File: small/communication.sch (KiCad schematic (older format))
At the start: 10 parts, among them J5 Conn_02x04_Odd_Even, U9 ISO1540

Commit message: simcard colder changed to 78800-0001
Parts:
- C27, C28: LCSC (none) -> C14663
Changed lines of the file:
@@
 F 5 "0,019 €" H 3100 3300 50  0001 C CNN "Price"
 F 6 "Mouser" H 3100 3300 50  0001 C CNN "Website"
+F 7 "C14663" H 3100 3300 50  0001 C CNN "LCSC"
 	1    3100 3300
 	1    0    0    -1
@@
 F 5 "0,019 €" H 5675 2875 50  0001 C CNN "Price"
 F 6 "Mouser" H 5675 2875 50  0001 C CNN "Website"
+F 7 "C14663" H 5675 2875 50  0001 C CNN "LCSC"
 	1    5675 2875
 	1    0    0    -1

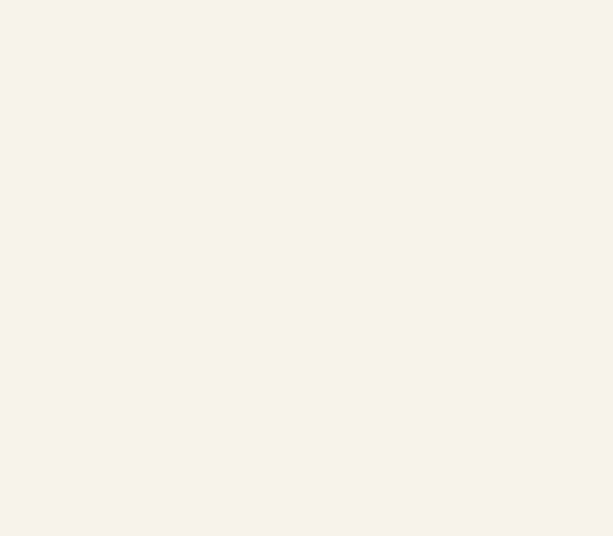
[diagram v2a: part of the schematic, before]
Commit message: connector rotated.
added rs485 output.

TODO: add bluetooth port.
check all parts
preaper bom list
prepare mouser list
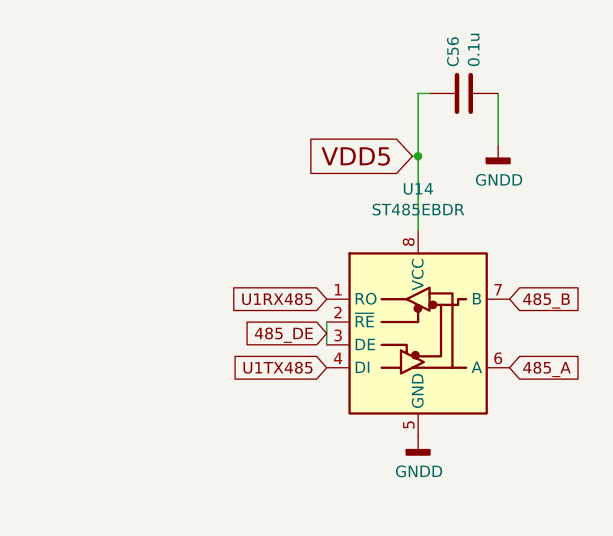
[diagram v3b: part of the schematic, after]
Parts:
- added C56: 0.1u, Capacitor_SMD:C_0603_1608Metric, symbol Device:C
- added U14: ST485EBDR, Package_SO:SOIC-8_3.9x4.9mm_P1.27mm, symbol Interface_UART:ST485EBDR
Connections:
- net GNDD: now also C56.2, U14.5 (GND)
- net VDD5: now also C56.1, U14.8 (VCC)
- new net 485_A: U14.6 (A)
- new net 485_B: U14.7 (B)
- new net 485_DE: U14.2 (~RE), U14.3 (DE)
- new net U1RX485: U14.1 (RO)
- new net U1TX485: U14.4 (DI)
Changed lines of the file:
@@
 	1    0    0    -1
 $EndComp
+$Comp
+L Interface_UART:ST485EBDR U14
+U 1 1 606D84B9
+P 8350 2825
+F 0 "U14" H 8350 3406 50  0000 C CNN
+F 1 "ST485EBDR" H 8350 3315 50  0000 C CNN
+F 2 "Package_SO:SOIC-8_3.9x4.9mm_P1.27mm" H 8350 1925 50  0001 C CNN
+F 3 "http://www.st.com/resource/en/datasheet/st485eb.pdf" H 8350 2875 50  0001 C CNN
+	1    8350 2825
+	1    0    0    -1
+$EndComp
+Text GLabel 7950 3025 0    50   Input ~ 0
+U1TX485
+Text GLabel 7950 2725 0    50   Input ~ 0
+U1RX485
+Wire Wire Line
+	7950 2925 7950 2825
+Text GLabel 7950 2875 0    50   Input ~ 0
+485_DE
+Text GLabel 8750 3025 2    50   Input ~ 0
+485_A
+Text GLabel 8750 2725 2    50   Input ~ 0
+485_B
+$Comp
+L power:GNDD #PWR0124
+U 1 1 606E725A
+P 8350 3325
+F 0 "#PWR0124" H 8350 3075 50  0001 C CNN
+F 1 "GNDD" H 8354 3170 50  0000 C CNN
+F 2 "" H 8350 3325 50  0001 C CNN
+F 3 "" H 8350 3325 50  0001 C CNN
+	1    8350 3325
+	1    0    0    -1
+$EndComp
+Text GLabel 8325 2100 0    79   Input ~ 0
+VDD5
+$Comp
+L power:GNDD #PWR0185
+U 1 1 606EB876
+P 8700 2050
+F 0 "#PWR0185" H 8700 1800 50  0001 C CNN
+F 1 "GNDD" H 8704 1895 50  0000 C CNN
+F 2 "" H 8700 2050 50  0001 C CNN
+F 3 "" H 8700 2050 50  0001 C CNN
+	1    8700 2050
+	1    0    0    -1
+$EndComp
+Wire Wire Line
+	8700 1825 8700 2050
+$Comp
+L Device:C C?
+U 1 1 606EAE77
+P 8550 1825
+AR Path="/606EAE77" Ref="C?"  Part="1"
+AR Path="/608144C5/606EAE77" Ref="C56"  Part="1"
+F 0 "C56" H 8665 1871 50  0000 L CNN
+F 1 "0.1u" H 8665 1780 50  0000 L CNN
+F 2 "Capacitor_SMD:C_0603_1608Metric" H 8588 1675 50  0001 C CNN
+F 3 "https://eu.mouser.com/datasheet/2/445/885012207098-1727748.pdf" H 8550 1825 50  0001 C CNN
+F 4 "885012207098" H 8550 1825 50  0001 C CNN "Mpn"
+F 5 "0,019 €" H 8550 1825 50  0001 C CNN "Price"
+F 6 "Mouser" H 8550 1825 50  0001 C CNN "Website"
+F 7 "C14663" H 8550 1825 50  0001 C CNN "LCSC"
+	1    8550 1825
+	0    -1   -1   0
+$EndComp
+Wire Wire Line
+	8350 2100 8325 2100
+Wire Wire Line
+	8350 2425 8350 2100
+Wire Wire Line
+	8350 2100 8350 1825
+Wire Wire Line
+	8350 1825 8400 1825
+Connection ~ 8350 2100
 $EndSCHEMATC

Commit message: GPS connector moved,
antenna matching networks removed

SUPERCAPACITOR from jlpcb used.
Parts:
- added D14: PSM712-LF-T7, Package_TO_SOT_SMD:SOT-23, symbol Diode:SM712_SOT23
- added JP3: Jumper, Jumper:SolderJumper-2_P1.3mm_Open_RoundedPad1.0x1.5mm, symbol Device:Jumper
- R12: value R -> 120
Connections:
- net 485_A: now also R12.2, D14.1 (A1)
- net 485_B: now also R12.1, D14.2 (A2)
- net GND_ISO: no longer C28.2, J5.7 (Pin_7)
- net SCL_ISO: no longer J5.5 (Pin_5)
- net SDA_ISO: no longer J5.3 (Pin_3)
- net VDD5: now also C28.1, J5.1 (Pin_1), JP3.1; no longer R12.1
- net VDD_ISO: now also JP3.2; no longer C28.1, J5.1 (Pin_1), R12.2
- net GNDD renamed GND
- net GND: now also C28.2, J5.3 (Pin_3), D14.3 (common)
- net SCL1 renamed SCL2
- net SDA1 renamed SDA2
- new net U2RX: J5.5 (Pin_5)
- new net U2TX: J5.7 (Pin_7)
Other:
- moved on the sheet: C28
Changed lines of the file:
@@
 Wire Wire Line
 	4125 2725 4375 2725
-Wire Wire Line
-	4375 2725 4375 2625
-$Comp
-L Device:R R?
-U 1 1 60818F85
-P 4375 2475
-AR Path="/60818F85" Ref="R?"  Part="1"
-AR Path="/608144C5/60818F85" Ref="R12"  Part="1"
-F 0 "R12" H 4445 2521 50  0000 L CNN
-F 1 "R" H 4445 2430 50  0000 L CNN
-F 2 "Resistor_SMD:R_0805_2012Metric" V 4305 2475 50  0001 C CNN
-F 3 "" H 4375 2475 50  0001 C CNN
-	1    4375 2475
-	1    0    0    -1
-$EndComp
 Connection ~ 4375 3025
 Connection ~ 4375 2725
@@
 Text Label 4450 2925 0    50   ~ 0
 SCL_ISO
-$Comp
-L Connector_Generic:Conn_02x04_Odd_Even J?
-U 1 1 60818F91
-P 5150 2825
-AR Path="/60818F91" Ref="J?"  Part="1"
-AR Path="/608144C5/60818F91" Ref="J5"  Part="1"
-F 0 "J5" H 5200 3142 50  0000 C CNN
-F 1 "Conn_02x04_Odd_Even" H 5200 3051 50  0000 C CNN
-F 2 "Connector_PinHeader_2.54mm:PinHeader_2x04_P2.54mm_Vertical" H 5150 2825 50  0001 C CNN
-F 3 "~" H 5150 2825 50  0001 C CNN
-F 4 "Connector unknown" H 5150 2825 50  0001 C CNN "Mpn"
-	1    5150 2825
-	1    0    0    -1
-$EndComp
-Wire Wire Line
-	5450 2725 4950 2725
 Wire Wire Line
 	4375 2725 4950 2725
-Connection ~ 4950 2725
 Wire Wire Line
 	4125 2825 4775 2825
 Wire Wire Line
-	4950 2825 5450 2825
-Connection ~ 4950 2825
-Wire Wire Line
 	4125 2925 4850 2925
 Wire Wire Line
-	4950 2925 5450 2925
-Connection ~ 4950 2925
-Wire Wire Line
-	5450 3025 4950 3025
-Wire Wire Line
 	4375 3025 4950 3025
-Connection ~ 4950 3025
 Text Notes 5050 2450 0    50   ~ 0
 i2c-iso
@@
 L Device:C C?
 U 1 1 60818FB1
-P 5675 2875
+P 6175 2875
 AR Path="/60818FB1" Ref="C?"  Part="1"
 AR Path="/608144C5/60818FB1" Ref="C28"  Part="1"
-F 0 "C28" H 5790 2921 50  0000 L CNN
-F 1 "0.1u" H 5790 2830 50  0000 L CNN
-F 2 "Capacitor_SMD:C_0603_1608Metric" H 5713 2725 50  0001 C CNN
-F 3 "https://eu.mouser.com/datasheet/2/445/885012207098-1727748.pdf" H 5675 2875 50  0001 C CNN
-F 4 "885012207098" H 5675 2875 50  0001 C CNN "Mpn"
-F 5 "0,019 €" H 5675 2875 50  0001 C CNN "Price"
-F 6 "Mouser" H 5675 2875 50  0001 C CNN "Website"
-F 7 "C14663" H 5675 2875 50  0001 C CNN "LCSC"
-	1    5675 2875
-	1    0    0    -1
-$EndComp
-Wire Wire Line
-	5450 2725 5675 2725
-Connection ~ 5450 2725
-Wire Wire Line
-	5675 3025 5450 3025
-Connection ~ 5450 3025
+F 0 "C28" H 6290 2921 50  0000 L CNN
+F 1 "0.1u" H 6290 2830 50  0000 L CNN
+F 2 "Capacitor_SMD:C_0603_1608Metric" H 6213 2725 50  0001 C CNN
+F 3 "https://eu.mouser.com/datasheet/2/445/885012207098-1727748.pdf" H 6175 2875 50  0001 C CNN
+F 4 "885012207098" H 6175 2875 50  0001 C CNN "Mpn"
+F 5 "0,019 €" H 6175 2875 50  0001 C CNN "Price"
+F 6 "Mouser" H 6175 2875 50  0001 C CNN "Website"
+F 7 "C14663" H 6175 2875 50  0001 C CNN "LCSC"
+	1    6175 2875
+	1    0    0    -1
+$EndComp
 Wire Wire Line
 	4775 2825 4775 2375
@@
 	4775 2825 4950 2825
 Wire Wire Line
-	4850 2925 4850 2450
+	4850 2925 4850 2575
 Connection ~ 4850 2925
 Wire Wire Line
@@
 	1    0    0    -1
 $EndComp
-Wire Wire Line
-	4850 2450 4900 2450
-Wire Wire Line
-	4900 2450 4900 2375
 Connection ~ 3100 3450
 Wire Wire Line
@@
 	3100 2725 3100 3150
 Text GLabel 2825 2825 0    50   Input ~ 0
-SDA1
+SDA2
 Text GLabel 2825 2925 0    50   Input ~ 0
-SCL1
-Wire Wire Line
-	4375 2325 4375 2075
+SCL2
 Wire Wire Line
 	4375 2075 4775 2075
@@
 Text GLabel 7950 2875 0    50   Input ~ 0
 485_DE
-Text GLabel 8750 3025 2    50   Input ~ 0
+Text GLabel 9525 3025 2    50   Input ~ 0
 485_A
-Text GLabel 8750 2725 2    50   Input ~ 0
+Text GLabel 9525 2725 2    50   Input ~ 0
 485_B
 $Comp
@@
 	8350 1825 8400 1825
 Connection ~ 8350 2100
+$Comp
+L Device:Jumper JP3
+U 1 1 602848D0
+P 4375 2425
+F 0 "JP3" V 4329 2552 50  0000 L CNN
+F 1 "Jumper" V 4420 2552 50  0000 L CNN
+F 2 "Jumper:SolderJumper-2_P1.3mm_Open_RoundedPad1.0x1.5mm" H 4375 2425 50  0001 C CNN
+F 3 "~" H 4375 2425 50  0001 C CNN
+	1    4375 2425
+	0    1    1    0
+$EndComp
+Wire Wire Line
+	4375 2125 4375 2075
+Wire Wire Line
+	4900 2075 5450 2075
+Wire Wire Line
+	5450 2075 5450 2725
+Connection ~ 4900 2075
+Wire Wire Line
+	5950 2825 5950 3025
+Wire Wire Line
+	5950 3025 6175 3025
+$Comp
+L power:GNDD #PWR0187
+U 1 1 6028DDBE
+P 6175 3025
+F 0 "#PWR0187" H 6175 2775 50  0001 C CNN
+F 1 "GNDD" H 6179 2870 50  0000 C CNN
+F 2 "" H 6175 3025 50  0001 C CNN
+F 3 "" H 6175 3025 50  0001 C CNN
+	1    6175 3025
+	1    0    0    -1
+$EndComp
+Connection ~ 6175 3025
+Wire Wire Line
+	5450 2825 5950 2825
+Wire Wire Line
+	5450 2725 6175 2725
+Text GLabel 5450 3025 2    50   Input ~ 0
+U2TX
+Text GLabel 5450 2925 2    50   Input ~ 0
+U2RX
+$Comp
+L Connector_Generic:Conn_02x04_Odd_Even J?
+U 1 1 60818F91
+P 5250 2825
+AR Path="/60818F91" Ref="J?"  Part="1"
+AR Path="/608144C5/60818F91" Ref="J5"  Part="1"
+F 0 "J5" H 5300 3142 50  0000 C CNN
+F 1 "Conn_02x04_Odd_Even" H 5300 3051 50  0000 C CNN
+F 2 "Connector_PinHeader_2.54mm:PinHeader_2x04_P2.54mm_Vertical" H 5250 2825 50  0001 C CNN
+F 3 "~" H 5250 2825 50  0001 C CNN
+F 4 "Connector unknown" H 5250 2825 50  0001 C CNN "Mpn"
+	1    5250 2825
+	-1   0    0    -1
+$EndComp
+Connection ~ 5450 2725
+$Comp
+L power:GND #PWR0188
+U 1 1 60296547
+P 3600 1800
+F 0 "#PWR0188" H 3600 1550 50  0001 C CNN
+F 1 "GND" H 3605 1627 50  0000 C CNN
+F 2 "" H 3600 1800 50  0001 C CNN
+F 3 "" H 3600 1800 50  0001 C CNN
+	1    3600 1800
+	1    0    0    -1
+$EndComp
+$Comp
+L power:GNDD #PWR0189
+U 1 1 60296AF3
+P 3825 1800
+F 0 "#PWR0189" H 3825 1550 50  0001 C CNN
+F 1 "GNDD" H 3829 1645 50  0000 C CNN
+F 2 "" H 3825 1800 50  0001 C CNN
+F 3 "" H 3825 1800 50  0001 C CNN
+	1    3825 1800
+	1    0    0    -1
+$EndComp
+Wire Wire Line
+	3825 1800 3600 1800
+$Comp
+L Device:R R12
+U 1 1 6035DB1F
+P 9250 2875
+F 0 "R12" H 9320 2921 50  0000 L CNN
+F 1 "120" H 9320 2830 50  0000 L CNN
+F 2 "Resistor_SMD:R_0805_2012Metric" V 9180 2875 50  0001 C CNN
+F 3 "https://datasheet.lcsc.com/szlcsc/Uniroyal-Elec-0805W8F1200T5E_C17437.pdf" H 9250 2875 50  0001 C CNN
+	1    9250 2875
+	1    0    0    -1
+$EndComp
+Wire Wire Line
+	8750 2725 9250 2725
+Connection ~ 9250 2725
+Wire Wire Line
+	9250 2725 9475 2725
+Wire Wire Line
+	9525 3025 9250 3025
+Connection ~ 9250 3025
+Wire Wire Line
+	9250 3025 8775 3025
+$Comp
+L Diode:SM712_SOT23 D14
+U 1 1 603613E9
+P 9125 3425
+F 0 "D14" H 9125 3641 50  0000 C CNN
+F 1 "PSM712-LF-T7" H 9125 3550 50  0000 C CNN
+F 2 "Package_TO_SOT_SMD:SOT-23" H 9125 3075 50  0001 C CNN
+F 3 "https://datasheet.lcsc.com/szlcsc/ProTek-Devices-PSM712-LF-T7_C32677.pdf" H 8975 3425 50  0001 C CNN
+F 4 "C32677" H 9125 3425 50  0001 C CNN "LCSC"
+F 5 "0.3704" H 9125 3425 50  0001 C CNN "Price"
+F 6 "PSM712-LF-T7" H 9125 3425 50  0001 C CNN "MPN"
+	1    9125 3425
+	1    0    0    -1
+$EndComp
+$Comp
+L power:GNDD #PWR0184
+U 1 1 60362763
+P 9125 3650
+F 0 "#PWR0184" H 9125 3400 50  0001 C CNN
+F 1 "GNDD" H 9129 3495 50  0000 C CNN
+F 2 "" H 9125 3650 50  0001 C CNN
+F 3 "" H 9125 3650 50  0001 C CNN
+	1    9125 3650
+	1    0    0    -1
+$EndComp
+Wire Wire Line
+	9125 3575 9125 3650
+Wire Wire Line
+	8775 3425 8775 3025
+Connection ~ 8775 3025
+Wire Wire Line
+	8775 3025 8750 3025
+Wire Wire Line
+	9475 3425 9475 2725
+Connection ~ 9475 2725
+Wire Wire Line
+	9475 2725 9525 2725
+Wire Wire Line
+	4900 2575 4850 2575
+Wire Wire Line
+	4900 2375 4900 2575
 $EndSCHEMATC

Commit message: BOM updated
Layout changed
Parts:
- C27, C28, C56: MPN (none) -> CC0603KRX7R9BB104; Price 0,019 € -> 0.0071; Website Mouser -> (none); source (none) -> 0
- D14, R11, R8: source (none) -> 0
- R12: LCSC (none) -> C17437; MPN (none) -> 0805W8F1200T5E; Price (none) -> 0.0037; source (none) -> 0
- R15: LCSC (none) -> C17513; MPN (none) -> 0805W8F1001T5E; Price (none) -> 0.0040; source (none) -> 0
- R16: LCSC (none) -> C17513; MPN (none) -> 0805W8F1001T5E; Mpn CRCW08051K00FKEAC -> 0805W8F1001T5E; Price 0.02 -> 0.0040; Website mouser -> (none); source (none) -> 0
- R17: LCSC (none) -> C17513; MPN (none) -> 0805W8F1001T5E; Price 0.02 -> 0.0040; Website mouser -> (none); source (none) -> 0
- U14: LCSC (none) -> C81186; MPN (none) -> ST485EBDR; source (none) -> 1
- U9: MPN (none) -> ISO1540DR; Mpn ISO1540DR -> (none); Website mouser -> (none); source (none) -> 1
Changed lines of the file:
@@
 F 2 "Package_SO:SOIC-8_3.9x4.9mm_P1.27mm" H 3725 2475 50  0001 C CNN
 F 3 "http://www.ti.com/general/docs/suppproductinfo.tsp?distId=26&gotoUrl=http%3A%2F%2Fwww.ti.com%2Flit%2Fgpn%2Fiso1540-q1" H 3725 2875 50  0001 C CNN
-F 4 "ISO1540DR" H 3725 2825 50  0001 C CNN "Mpn"
+F 4 "" H 3725 2825 50  0001 C CNN "Mpn"
 F 5 "1.6046" H 3725 2825 50  0001 C CNN "Price"
-F 6 "mouser" H 3725 2825 50  0001 C CNN "Website"
+F 6 "" H 3725 2825 50  0001 C CNN "Website"
 F 7 " C179739" H 3725 2825 50  0001 C CNN "LCSC"
+F 8 "ISO1540DR" H 3725 2825 50  0001 C CNN "MPN"
+F 9 "1" H 3725 2825 50  0001 C CNN "source"
 	1    3725 2825
 	1    0    0    -1
@@
 F 1 "R" H 4445 3280 50  0000 L CNN
 F 2 "Resistor_SMD:R_0805_2012Metric" V 4305 3325 50  0001 C CNN
-F 3 "" H 4375 3325 50  0001 C CNN
+F 3 "https://datasheet.lcsc.com/szlcsc/Uniroyal-Elec-0805W8F1001T5E_C17513.pdf" H 4375 3325 50  0001 C CNN
+F 4 "C17513" H 4375 3325 50  0001 C CNN "LCSC"
+F 5 "0805W8F1001T5E" H 4375 3325 50  0001 C CNN "MPN"
+F 6 "0.0040" H 4375 3325 50  0001 C CNN "Price"
+F 7 "0" H 4375 3325 50  0001 C CNN "source"
 	1    4375 3325
 	1    0    0    -1
@@
 F 3 "https://eu.mouser.com/datasheet/2/445/885012207098-1727748.pdf" H 3100 3300 50  0001 C CNN
 F 4 "885012207098" H 3100 3300 50  0001 C CNN "Mpn"
-F 5 "0,019 €" H 3100 3300 50  0001 C CNN "Price"
-F 6 "Mouser" H 3100 3300 50  0001 C CNN "Website"
+F 5 "0.0071" H 3100 3300 50  0001 C CNN "Price"
+F 6 "" H 3100 3300 50  0001 C CNN "Website"
 F 7 "C14663" H 3100 3300 50  0001 C CNN "LCSC"
+F 8 "CC0603KRX7R9BB104" H 3100 3300 50  0001 C CNN "MPN"
+F 9 "0" H 3100 3300 50  0001 C CNN "source"
 	1    3100 3300
 	1    0    0    -1
@@
 F 3 "https://eu.mouser.com/datasheet/2/445/885012207098-1727748.pdf" H 6175 2875 50  0001 C CNN
 F 4 "885012207098" H 6175 2875 50  0001 C CNN "Mpn"
-F 5 "0,019 €" H 6175 2875 50  0001 C CNN "Price"
-F 6 "Mouser" H 6175 2875 50  0001 C CNN "Website"
+F 5 "0.0071" H 6175 2875 50  0001 C CNN "Price"
+F 6 "" H 6175 2875 50  0001 C CNN "Website"
 F 7 "C14663" H 6175 2875 50  0001 C CNN "LCSC"
+F 8 "CC0603KRX7R9BB104" H 6175 2875 50  0001 C CNN "MPN"
+F 9 "0" H 6175 2875 50  0001 C CNN "source"
 	1    6175 2875
 	1    0    0    -1
@@
 F 1 "1k" H 4625 2175 50  0000 L CNN
 F 2 "Resistor_SMD:R_0805_2012Metric" V 4705 2225 50  0001 C CNN
-F 3 "https://eu.mouser.com/datasheet/2/427/crcwce3-1762584.pdf" H 4775 2225 50  0001 C CNN
-F 4 "CRCW08051K00FKEAC" H 4775 2225 50  0001 C CNN "Mpn"
-F 5 "0.02" H 4775 2225 50  0001 C CNN "Price"
-F 6 "mouser" H 4775 2225 50  0001 C CNN "Website"
+F 3 "https://datasheet.lcsc.com/szlcsc/Uniroyal-Elec-0805W8F1001T5E_C17513.pdf" H 4775 2225 50  0001 C CNN
+F 4 "0805W8F1001T5E" H 4775 2225 50  0001 C CNN "Mpn"
+F 5 "0.0040" H 4775 2225 50  0001 C CNN "Price"
+F 6 "" H 4775 2225 50  0001 C CNN "Website"
+F 7 "C17513" H 4775 2225 50  0001 C CNN "LCSC"
+F 8 "0805W8F1001T5E" H 4775 2225 50  0001 C CNN "MPN"
+F 9 "0" H 4775 2225 50  0001 C CNN "source"
 	1    4775 2225
 	1    0    0    -1
@@
 F 1 "1k" H 4975 2175 50  0000 L CNN
 F 2 "Resistor_SMD:R_0805_2012Metric" V 4830 2225 50  0001 C CNN
-F 3 "https://eu.mouser.com/datasheet/2/427/crcwce3-1762584.pdf" H 4900 2225 50  0001 C CNN
+F 3 "https://datasheet.lcsc.com/szlcsc/Uniroyal-Elec-0805W8F1001T5E_C17513.pdf" H 4900 2225 50  0001 C CNN
 F 4 "CRCW08051K00FKEAC" H 4900 2225 50  0001 C CNN "Mpn"
-F 5 "0.02" H 4900 2225 50  0001 C CNN "Price"
-F 6 "mouser" H 4900 2225 50  0001 C CNN "Website"
+F 5 "0.0040" H 4900 2225 50  0001 C CNN "Price"
+F 6 "" H 4900 2225 50  0001 C CNN "Website"
+F 7 "C17513" H 4900 2225 50  0001 C CNN "LCSC"
+F 8 "0805W8F1001T5E" H 4900 2225 50  0001 C CNN "MPN"
+F 9 "0" H 4900 2225 50  0001 C CNN "source"
 	1    4900 2225
 	1    0    0    -1
@@
 F 5 "0603WAF2701T5E" H 2850 2075 50  0001 C CNN "MPN"
 F 6 "0.0023" H 2850 2075 50  0001 C CNN "Price"
+F 7 "0" H 2850 2075 50  0001 C CNN "source"
 	1    2850 2075
 	1    0    0    -1
@@
 F 5 "0603WAF2701T5E" H 2950 2075 50  0001 C CNN "MPN"
 F 6 "0.0023" H 2950 2075 50  0001 C CNN "Price"
+F 7 "0" H 2950 2075 50  0001 C CNN "source"
 	1    2950 2075
 	1    0    0    -1
@@
 F 2 "Package_SO:SOIC-8_3.9x4.9mm_P1.27mm" H 8350 1925 50  0001 C CNN
 F 3 "http://www.st.com/resource/en/datasheet/st485eb.pdf" H 8350 2875 50  0001 C CNN
+F 4 "C81186" H 8350 2825 50  0001 C CNN "LCSC"
+F 5 "ST485EBDR" H 8350 2825 50  0001 C CNN "MPN"
+F 6 "1" H 8350 2825 50  0001 C CNN "source"
 	1    8350 2825
 	1    0    0    -1
@@
 F 3 "https://eu.mouser.com/datasheet/2/445/885012207098-1727748.pdf" H 8550 1825 50  0001 C CNN
 F 4 "885012207098" H 8550 1825 50  0001 C CNN "Mpn"
-F 5 "0,019 €" H 8550 1825 50  0001 C CNN "Price"
-F 6 "Mouser" H 8550 1825 50  0001 C CNN "Website"
+F 5 "0.0071" H 8550 1825 50  0001 C CNN "Price"
+F 6 "" H 8550 1825 50  0001 C CNN "Website"
 F 7 "C14663" H 8550 1825 50  0001 C CNN "LCSC"
+F 8 "CC0603KRX7R9BB104" H 8550 1825 50  0001 C CNN "MPN"
+F 9 "0" H 8550 1825 50  0001 C CNN "source"
 	1    8550 1825
 	0    -1   -1   0
@@
 F 2 "Resistor_SMD:R_0805_2012Metric" V 9180 2875 50  0001 C CNN
 F 3 "https://datasheet.lcsc.com/szlcsc/Uniroyal-Elec-0805W8F1200T5E_C17437.pdf" H 9250 2875 50  0001 C CNN
+F 4 "C17437" H 9250 2875 50  0001 C CNN "LCSC"
+F 5 "0805W8F1200T5E" H 9250 2875 50  0001 C CNN "MPN"
+F 6 "0.0037" H 9250 2875 50  0001 C CNN "Price"
+F 7 "0" H 9250 2875 50  0001 C CNN "source"
 	1    9250 2875
 	1    0    0    -1
@@
 F 5 "0.3704" H 9125 3425 50  0001 C CNN "Price"
 F 6 "PSM712-LF-T7" H 9125 3425 50  0001 C CNN "MPN"
+F 7 "0" H 9125 3425 50  0001 C CNN "source"
 	1    9125 3425
 	1    0    0    -1

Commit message: minor updates
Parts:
- U14: Price (none) -> 0.4272
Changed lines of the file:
@@
 F 5 "ST485EBDR" H 8350 2825 50  0001 C CNN "MPN"
 F 6 "1" H 8350 2825 50  0001 C CNN "source"
+F 7 "0.4272" H 8350 2825 50  0001 C CNN "Price"
 	1    8350 2825
 	1    0    0    -1

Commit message: ENC28j60 package changed to soic 28 17.9
TODO: route
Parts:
- J5, JP3: LCSC (none) -> N/A
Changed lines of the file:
@@
 F 2 "Jumper:SolderJumper-2_P1.3mm_Open_RoundedPad1.0x1.5mm" H 4375 2425 50  0001 C CNN
 F 3 "~" H 4375 2425 50  0001 C CNN
+F 4 "N/A" H 4375 2425 50  0001 C CNN "LCSC"
 	1    4375 2425
 	0    1    1    0
@@
 F 3 "~" H 5250 2825 50  0001 C CNN
 F 4 "Connector unknown" H 5250 2825 50  0001 C CNN "Mpn"
+F 5 "N/A" H 5250 2825 50  0001 C CNN "LCSC"
 	1    5250 2825
 	-1   0    0    -1
